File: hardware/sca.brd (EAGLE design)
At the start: 87.6 x 73.3 mm, 30 parts

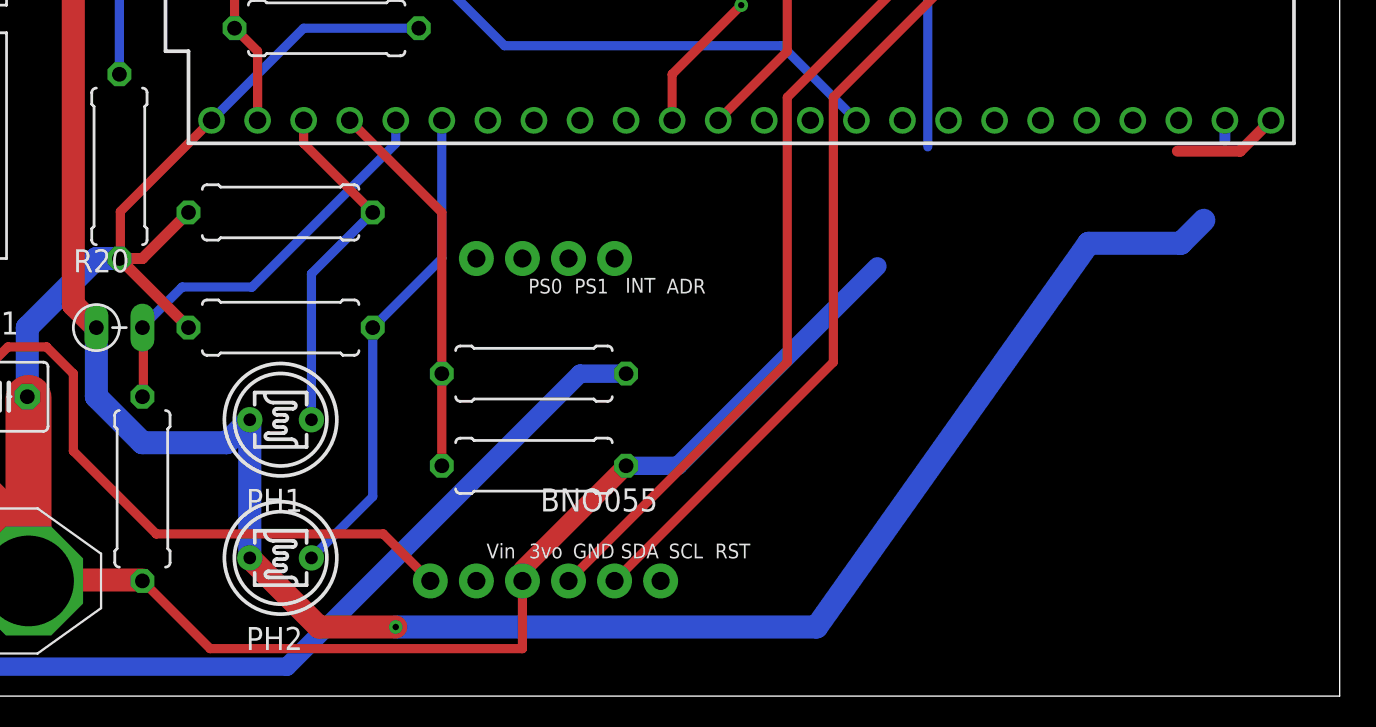
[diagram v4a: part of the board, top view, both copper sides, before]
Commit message: Added Decoupling Caps for Xbee per datasheet
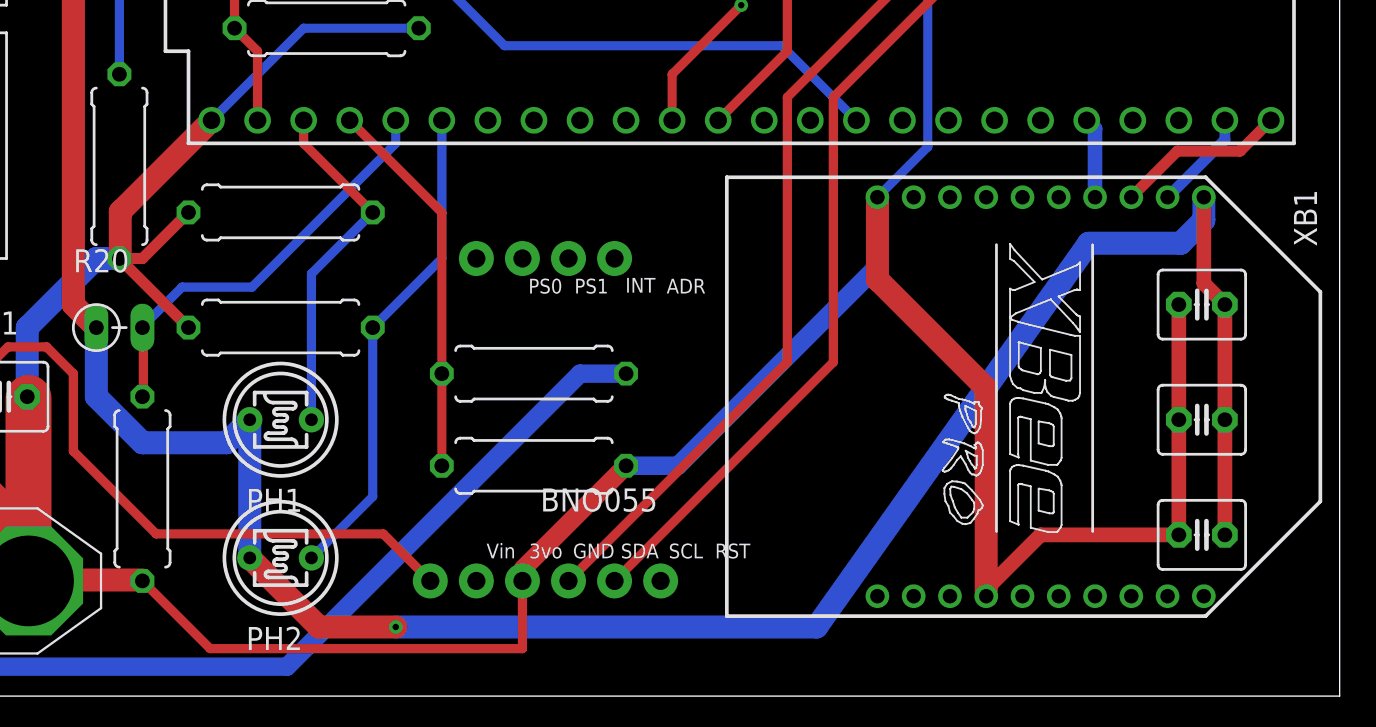
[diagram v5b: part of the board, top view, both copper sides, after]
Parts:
- added C1: 47pF, adafruit:C025-040X050
- added C2: 1uF, adafruit:C025-040X050
- added C3: 10uF, adafruit:C025-040X050
- added XB1: XBEE-PRO, maxstream:XBEE-PRO
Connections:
- new net XBEE_EN: U$9.28, XB1.4
- net +3V3: now also C1.1, C2.1, C3.1, XB1.1
- net GND: now also C1.2, C2.2, C3.2, XB1.10, XB1.14
- net XBEE_RX: now also XB1.3
- net XBEE_TX: now also XB1.2
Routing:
- net GND: track 316.9 -> 374.0 mm
- net +3V3: track 180.4 -> 200.8 mm
- net XBEE_TX: track 1.08 -> 5.55 mm
- net XBEE_EN: track 0.00 -> 4.43 mm
- net XBEE_RX: track 5.86 -> 9.46 mm
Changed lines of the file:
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@@
 <attribute name="NAME" x="17.78" y="23.368" size="1.27" layer="25" ratio="10"/>
+</element>
+<element name="XB1" library="maxstream" library_urn="urn:adsk.eagle:library:270" package="XBEE-PRO" package3d_urn="urn:adsk.eagle:package:18008/1" value="XBEE-PRO" x="71.12" y="16.51" smashed="yes" rot="R270">
+<attribute name="MF" value="" x="50.8" y="-8.89" size="1.778" layer="27" rot="R270" display="off"/>
+<attribute name="MPN" value="XBP24-AWI-001" x="50.8" y="-8.89" size="1.778" layer="27" rot="R270" display="off"/>
+<attribute name="NAME" x="85.09" y="27.94" size="1.27" layer="25" rot="R270"/>
+<attribute name="OC_FARNELL" value="1337916" x="50.8" y="-8.89" size="1.778" layer="27" rot="R270" display="off"/>
+<attribute name="OC_NEWARK" value="42M2667" x="50.8" y="-8.89" size="1.778" layer="27" rot="R270" display="off"/>
+<attribute name="VALUE" x="60.71" y="21.59" size="1.27" layer="27" rot="R270"/>
 </element>
 <element name="BNO055_H1" library="microbuilder" package="1X06_ROUND_76" value="" x="43.815" y="6.35" smashed="yes">
@@
 <element name="U$9" library="Teensy_3_and_LC_Series_Boards_v1.4" package="TEENSY_3.6_DIL" value="TEENSY_3.6_DIL" x="53.34" y="39.37" smashed="yes" rot="R90">
 <attribute name="VALUE" x="50.8" y="43.18" size="1.27" layer="27" font="vector" rot="R180"/>
+</element>
+<element name="C1" library="adafruit" library_urn="urn:adsk.eagle:library:420" package="C025-040X050" package3d_urn="urn:adsk.eagle:package:6240321/1" value="47pF" x="80.01" y="21.59" smashed="yes" rot="R180">
+<attribute name="VALUE" x="83.566" y="25.019" size="1.27" layer="27" ratio="10" rot="R180"/>
+</element>
+<element name="C2" library="adafruit" library_urn="urn:adsk.eagle:library:420" package="C025-040X050" package3d_urn="urn:adsk.eagle:package:6240321/1" value="1uF" x="80.01" y="15.24" smashed="yes" rot="R180">
+<attribute name="VALUE" x="82.296" y="18.669" size="1.27" layer="27" ratio="10" rot="R180"/>
+</element>
+<element name="C3" library="adafruit" library_urn="urn:adsk.eagle:library:420" package="C025-040X050" package3d_urn="urn:adsk.eagle:package:6240321/1" value="10uF" x="80.01" y="8.89" smashed="yes" rot="R180">
+<attribute name="VALUE" x="82.296" y="12.319" size="1.27" layer="27" ratio="10" rot="R180"/>
 </element>
 </elements>
@@
 <wire x1="63.1444" y1="49.276" x2="60.96" y2="47.0916" width="0.508" layer="1"/>
 <wire x1="60.96" y1="46.99" x2="60.96" y2="47.0916" width="0.508" layer="1"/>
-<wire x1="25.4" y1="31.75" x2="20.3708" y2="26.7208" width="0.508" layer="1"/>
-<wire x1="20.3708" y1="26.7208" x2="20.3708" y2="24.1554" width="0.508" layer="1"/>
+<wire x1="25.4" y1="31.75" x2="20.3708" y2="26.7208" width="1.27" layer="1"/>
+<wire x1="20.3708" y1="26.7208" x2="20.3708" y2="24.1554" width="1.27" layer="1"/>
 <wire x1="16.4592" y1="6.4008" x2="21.59" y2="6.4008" width="1.27" layer="1"/>
 <wire x1="21.59" y1="6.4008" x2="21.59" y2="6.35" width="0.508" layer="1"/>
@@
 <wire x1="25.3238" y1="2.6162" x2="21.59" y2="6.35" width="0.508" layer="1"/>
 <wire x1="42.545" y1="2.6162" x2="25.3238" y2="2.6162" width="0.508" layer="1"/>
-<wire x1="51.12" y1="12.7" x2="62.12" y2="23.7" width="1.016" layer="16"/>
+<wire x1="62.12" y1="23.7" x2="51.12" y2="12.7" width="1.016" layer="16"/>
 <wire x1="51.12" y1="12.7" x2="48.26" y2="12.7" width="1.016" layer="16"/>
 <wire x1="24.13" y1="26.67" x2="21.59" y2="24.13" width="0.6096" layer="1"/>
@@
 <wire x1="42.545" y1="6.35" x2="42.545" y2="2.6162" width="0.508" layer="1"/>
 <wire x1="64.897" y1="30.287" x2="64.897" y2="43.053" width="0.508" layer="16"/>
-<wire x1="62.12" y1="23.7" x2="64.897" y2="30.287" width="0" layer="19" extent="16-16"/>
+<contactref element="XB1" pad="10"/>
+<contactref element="XB1" pad="14"/>
+<wire x1="68.12" y1="5.51" x2="68.12" y2="16.97" width="1.27" layer="1"/>
+<wire x1="62.12" y1="22.97" x2="62.12" y2="27.51" width="1.27" layer="1"/>
+<wire x1="68.12" y1="16.97" x2="62.12" y2="22.97" width="1.27" layer="1"/>
+<wire x1="62.12" y1="27.51" x2="62.12" y2="23.7" width="1.016" layer="16"/>
+<wire x1="62.12" y1="27.51" x2="64.897" y2="30.287" width="0.508" layer="16"/>
+<contactref element="C1" pad="2"/>
+<contactref element="C2" pad="2"/>
+<contactref element="C3" pad="2"/>
+<wire x1="78.74" y1="8.89" x2="71.12" y2="8.89" width="0.8128" layer="1"/>
+<wire x1="71.12" y1="8.89" x2="68.12" y2="5.89" width="0.8128" layer="1"/>
+<wire x1="68.12" y1="5.89" x2="68.12" y2="5.51" width="0.8128" layer="1"/>
+<wire x1="78.74" y1="8.89" x2="78.74" y2="15.24" width="0.8128" layer="1"/>
+<wire x1="78.74" y1="21.59" x2="78.74" y2="15.24" width="0.8128" layer="1"/>
 </signal>
 <signal name="GPS_EN">
@@
 <contactref element="3V3_REG" pad="3"/>
 <contactref element="C13" pad="1"/>
+<contactref element="XB1" pad="1"/>
 <contactref element="BMP338_H" pad="1"/>
 <wire x1="6.35" y1="60.96" x2="3.81" y2="63.5" width="1.905" layer="1"/>
@@
 <wire x1="73.77" y1="24.97" x2="58.7656375" y2="3.81" width="1.27" layer="16"/>
 <wire x1="80.12" y1="26.24" x2="78.85" y2="24.97" width="1.27" layer="16"/>
+<wire x1="80.12" y1="26.24" x2="80.12" y2="27.51" width="1.27" layer="16"/>
 <wire x1="78.85" y1="24.97" x2="73.77" y2="24.97" width="1.27" layer="16"/>
 <wire x1="19.89" y1="57.15" x2="18.62" y2="55.88" width="1.27" layer="1"/>
@@
 <wire x1="31.32" y1="3.81" x2="35.56" y2="3.81" width="1.27" layer="1"/>
 <wire x1="18.62" y1="66.04" x2="18.62" y2="54.61" width="1.27" layer="1"/>
+<contactref element="C1" pad="1"/>
+<contactref element="C2" pad="1"/>
+<contactref element="C3" pad="1"/>
+<wire x1="81.28" y1="8.89" x2="81.28" y2="15.24" width="0.8128" layer="1"/>
+<wire x1="81.28" y1="21.59" x2="81.28" y2="15.24" width="0.8128" layer="1"/>
+<wire x1="81.28" y1="21.59" x2="80.12" y2="22.75" width="0.8128" layer="1"/>
+<wire x1="80.12" y1="22.75" x2="80.12" y2="27.51" width="0.8128" layer="1"/>
 </signal>
 <signal name="+5V">
@@
 <signal name="XBEE_TX">
 <contactref element="U$9" pad="31/A12"/>
+<contactref element="XB1" pad="2"/>
 <wire x1="81.28" y1="31.75" x2="81.28" y2="30.66996875" width="0.6096" layer="16"/>
+<wire x1="78.12" y1="27.51" x2="81.28" y2="30.66996875" width="0.6096" layer="16"/>
 </signal>
 <signal name="XBEE_RX">
 <contactref element="U$9" pad="32/A13"/>
+<contactref element="XB1" pad="3"/>
 <wire x1="82.12" y1="30.05" x2="78.66" y2="30.05" width="0.6096" layer="1"/>
+<wire x1="76.12" y1="27.51" x2="78.66" y2="30.05" width="0.6096" layer="1"/>
 <wire x1="82.12" y1="30.05" x2="83.82" y2="31.75" width="0.6096" layer="1"/>
 </signal>
@@
 <contactref element="BNO055_H1" pad="2"/>
 </signal>
+<signal name="XBEE_EN">
+<contactref element="XB1" pad="4"/>
+<contactref element="U$9" pad="28"/>
+<wire x1="73.66" y1="31.75" x2="74.12" y2="31.29" width="0.8128" layer="16"/>
+<wire x1="74.12" y1="31.29" x2="74.12" y2="27.51" width="0.8128" layer="16"/>
+</signal>
 </signals>

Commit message: added notes
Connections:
- new net XBEE_RST: U$9.27, XB1.5
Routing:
- net XBEE_RST: track 0.00 -> 4.65 mm
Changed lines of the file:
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@@
 <contactref element="C2" pad="2"/>
 <contactref element="C3" pad="2"/>
-<wire x1="78.74" y1="8.89" x2="71.12" y2="8.89" width="0.8128" layer="1"/>
-<wire x1="71.12" y1="8.89" x2="68.12" y2="5.89" width="0.8128" layer="1"/>
+<wire x1="78.74" y1="8.89" x2="71.12" y2="8.89" width="1.27" layer="1"/>
+<wire x1="71.12" y1="8.89" x2="68.12" y2="5.89" width="1.27" layer="1"/>
 <wire x1="68.12" y1="5.89" x2="68.12" y2="5.51" width="0.8128" layer="1"/>
-<wire x1="78.74" y1="8.89" x2="78.74" y2="15.24" width="0.8128" layer="1"/>
-<wire x1="78.74" y1="21.59" x2="78.74" y2="15.24" width="0.8128" layer="1"/>
+<wire x1="78.74" y1="8.89" x2="78.74" y2="15.24" width="1.27" layer="1"/>
+<wire x1="78.74" y1="21.59" x2="78.74" y2="15.24" width="1.27" layer="1"/>
 </signal>
 <signal name="GPS_EN">
@@
 <contactref element="C2" pad="1"/>
 <contactref element="C3" pad="1"/>
-<wire x1="81.28" y1="8.89" x2="81.28" y2="15.24" width="0.8128" layer="1"/>
-<wire x1="81.28" y1="21.59" x2="81.28" y2="15.24" width="0.8128" layer="1"/>
-<wire x1="81.28" y1="21.59" x2="80.12" y2="22.75" width="0.8128" layer="1"/>
-<wire x1="80.12" y1="22.75" x2="80.12" y2="27.51" width="0.8128" layer="1"/>
+<wire x1="81.28" y1="8.89" x2="81.28" y2="15.24" width="1.27" layer="1"/>
+<wire x1="81.28" y1="21.59" x2="81.28" y2="15.24" width="1.27" layer="1"/>
+<wire x1="81.28" y1="21.59" x2="80.12" y2="22.75" width="1.27" layer="1"/>
+<wire x1="80.12" y1="22.75" x2="80.12" y2="27.51" width="1.27" layer="1"/>
 </signal>
 <signal name="+5V">
@@
 <wire x1="74.12" y1="31.29" x2="74.12" y2="27.51" width="0.8128" layer="16"/>
 </signal>
+<signal name="XBEE_RST">
+<contactref element="XB1" pad="5"/>
+<contactref element="U$9" pad="27"/>
+<wire x1="72.12" y1="27.51" x2="72.12" y2="30.75" width="0.8128" layer="16"/>
+<wire x1="72.12" y1="30.75" x2="71.12" y2="31.75" width="0.8128" layer="16"/>
+</signal>
 </signals>

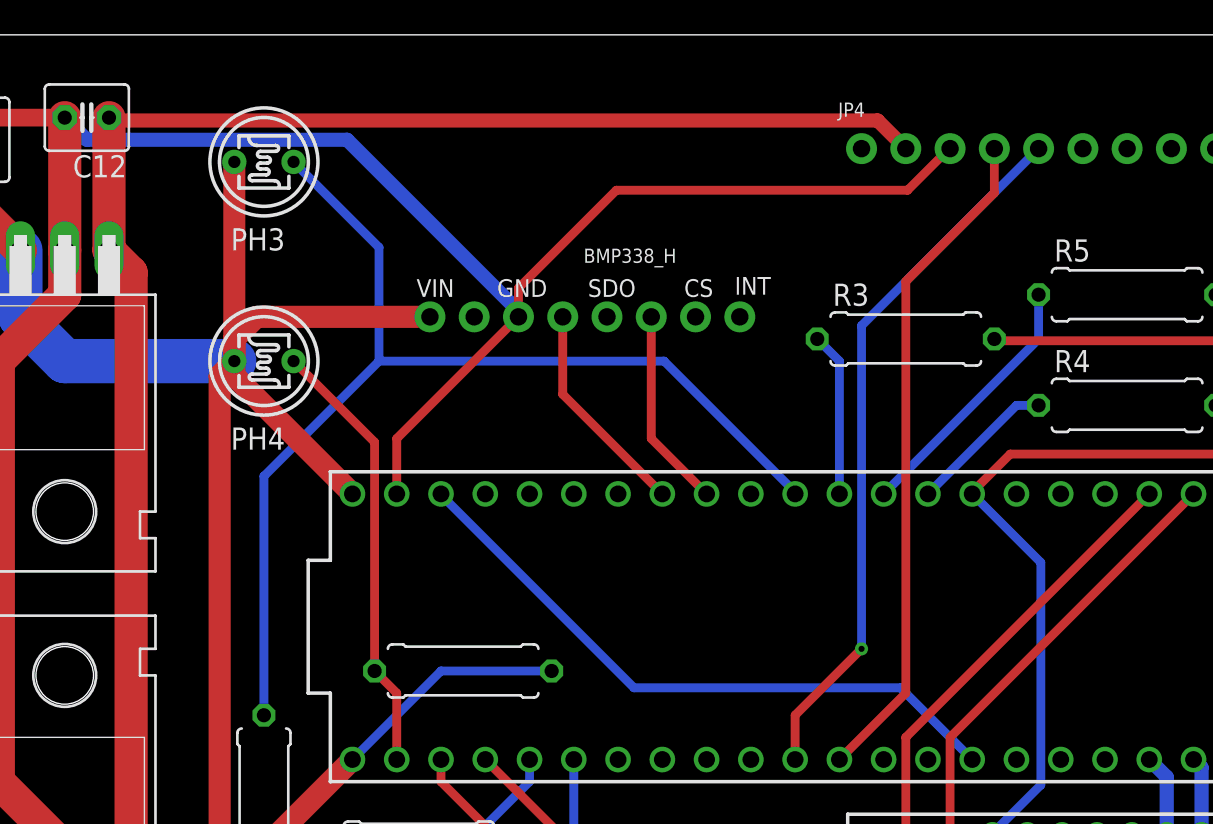
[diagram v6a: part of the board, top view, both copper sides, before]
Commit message: added 3.3 and 5 V dividers
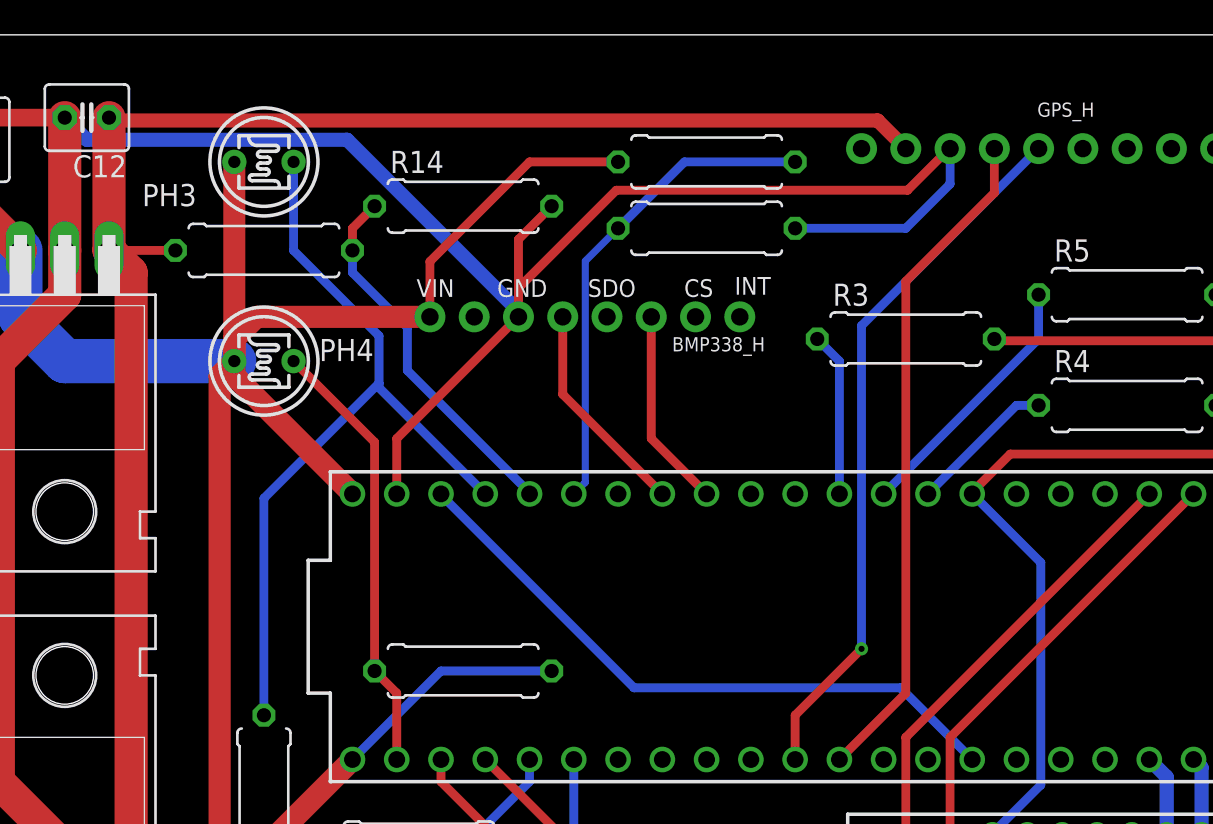
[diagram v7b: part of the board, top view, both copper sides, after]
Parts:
- added R11, R12, R13, R14: 1M, resistor:0309/10
- renumbered JP4 to GPS_H, U$9 to TEENSY3.6
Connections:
- net MCU_2 renamed BATT_V
- new net 3V3_V: R11.1, R12.1, TEENSY3.6.21/A7
- new net 5V_V: R13.1, R14.1, TEENSY3.6.22/A8
- net +3V3: now also R11.2
- net +5V: now also R13.2
- net GND: now also R12.2, R14.2
- net PR_3: now also TEENSY3.6.23/A9; no longer TEENSY3.6.16/A2
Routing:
- net 3V3_V: track 0.00 -> 28.0 mm
- net 5V_V: track 0.00 -> 21.2 mm
- net GND: track 374.0 -> 393.2 mm
- net PR_3: track 63.6 -> 45.4 mm
- net +3V3: track 200.8 -> 217.1 mm
- net +5V: track 134.5 -> 138.3 mm
